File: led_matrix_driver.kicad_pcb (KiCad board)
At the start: 4 copper layers, 41 parts, among them J1 Conn_02x17_Odd_Even, Q1 PXN020-100QSJ, Q2 TPH4R50ANH1,LQ, U1 LV5144RGYR, U2 Pico, U3 ESP32-WROOM-32, U4 74AHCT541, U5 74AHCT541

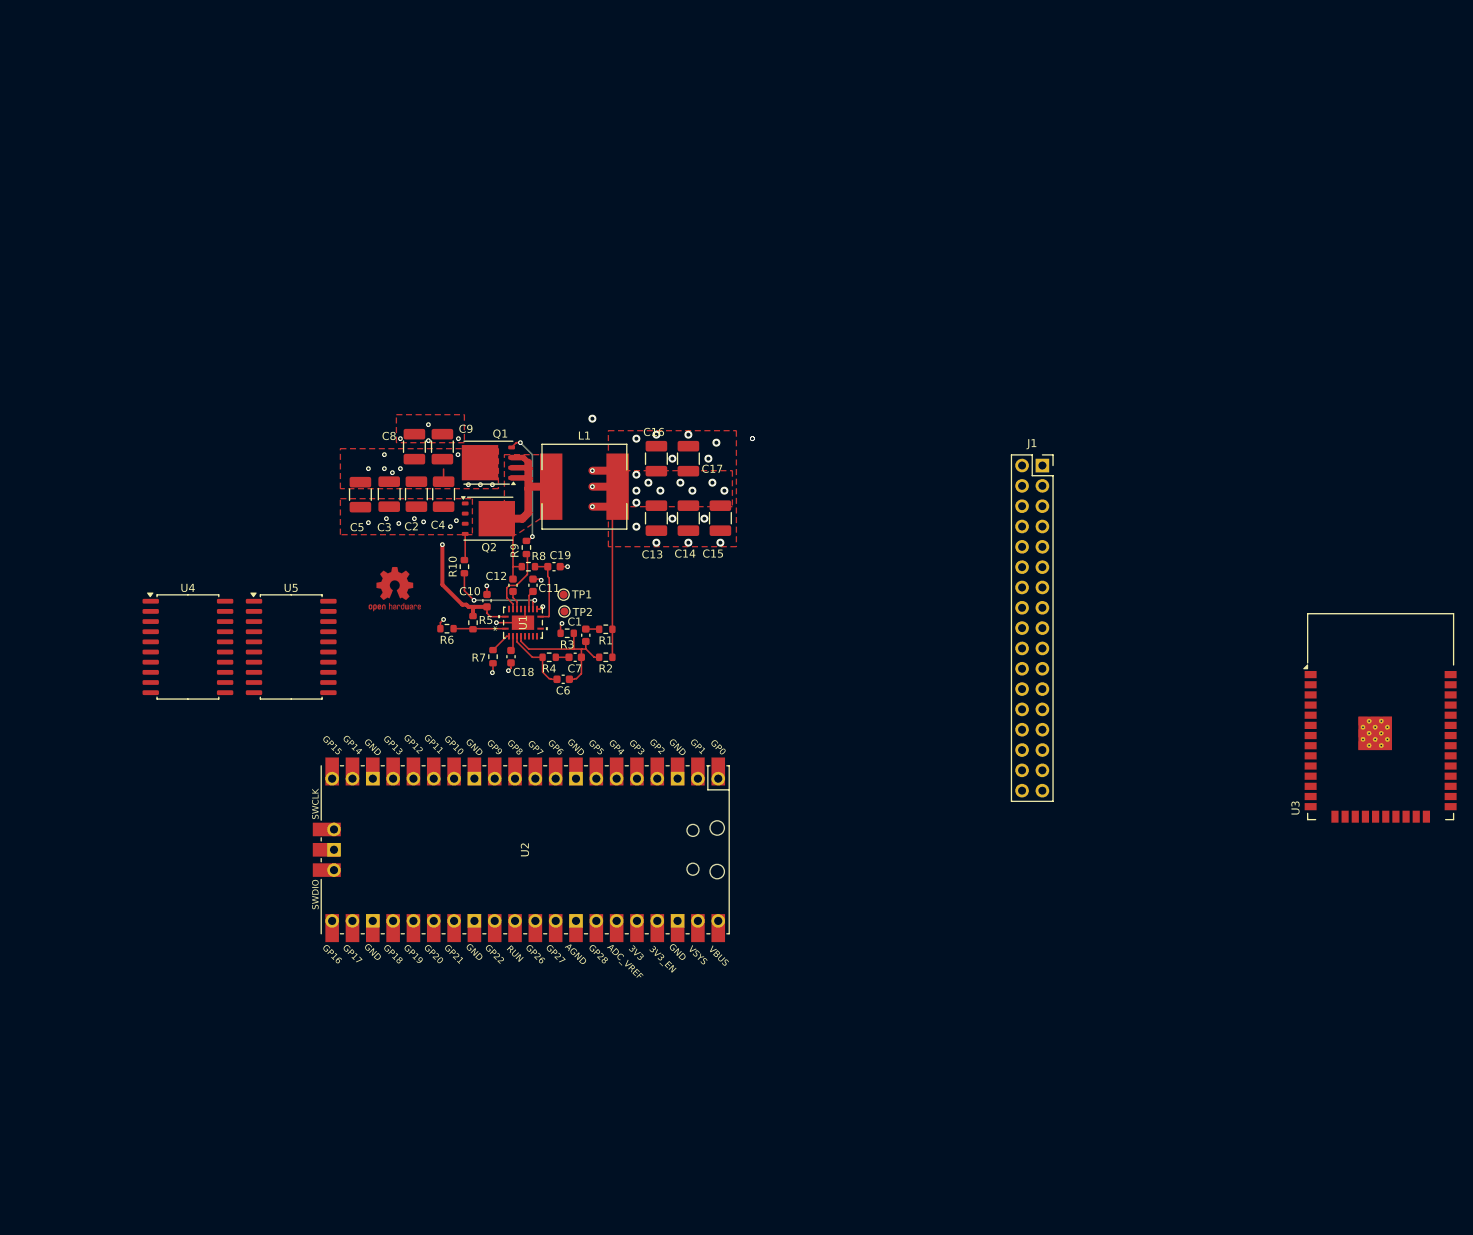
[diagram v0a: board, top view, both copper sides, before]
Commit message: Rearranged LED signals for easier layout
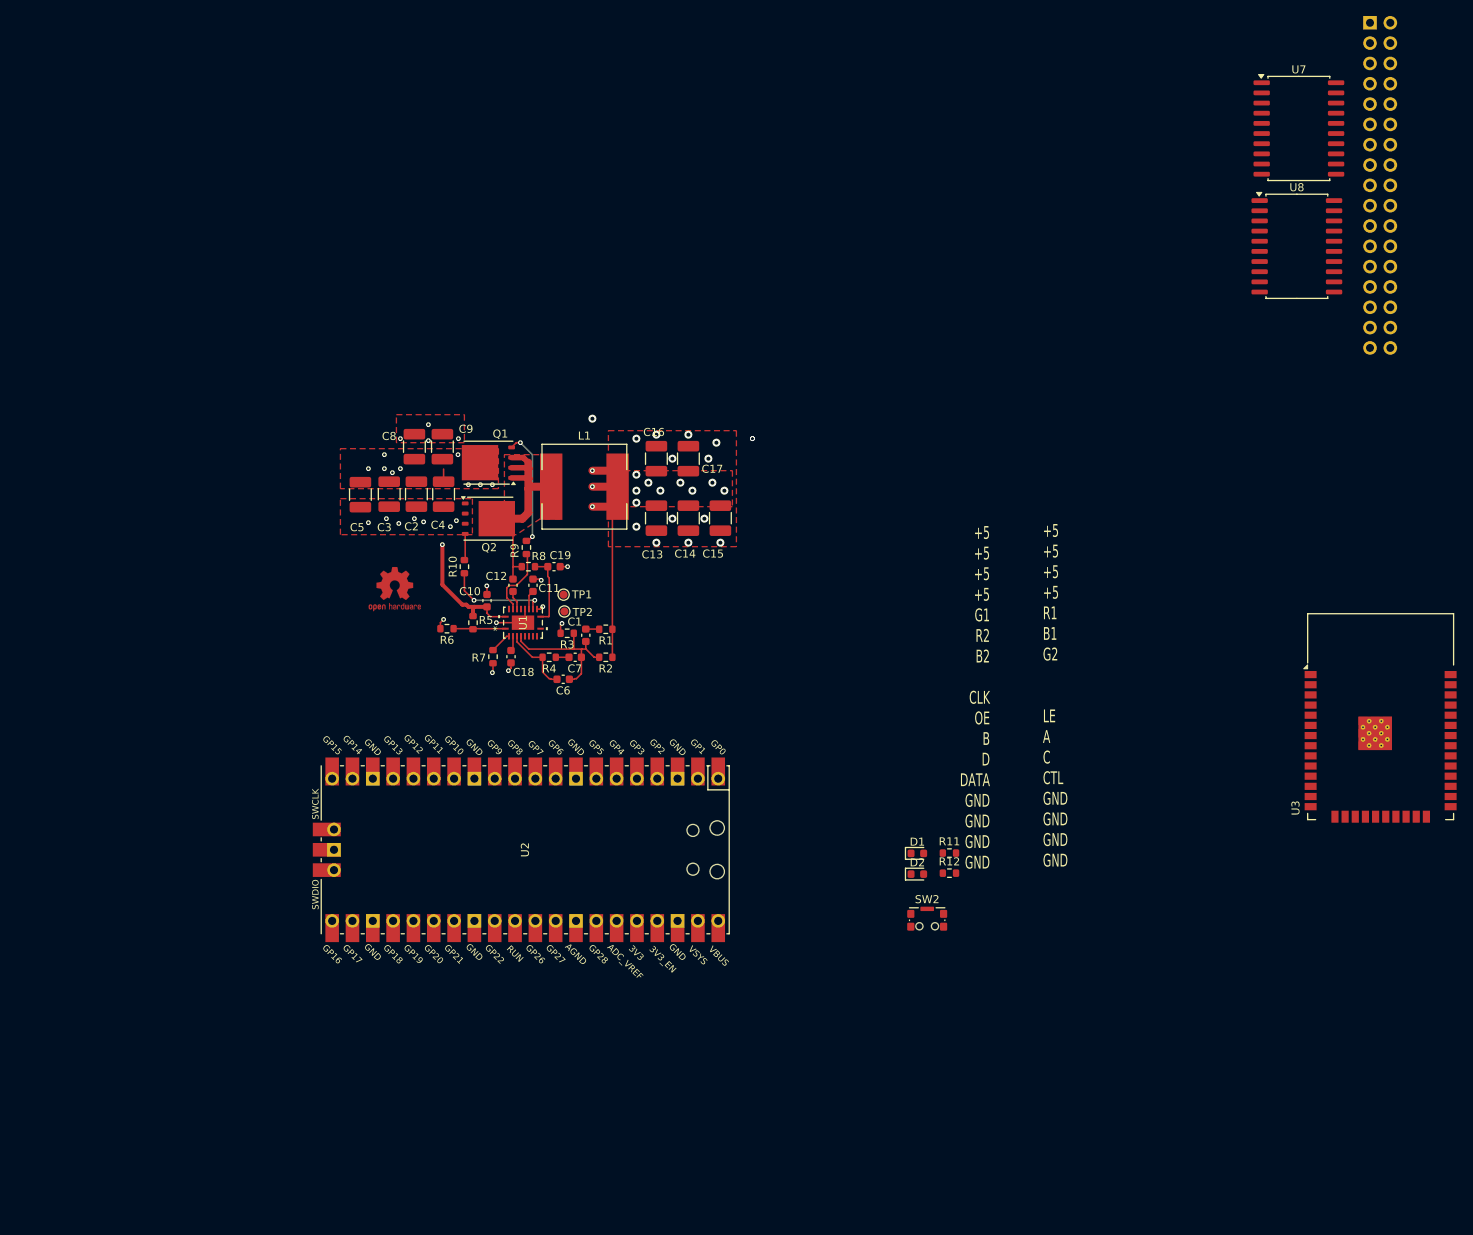
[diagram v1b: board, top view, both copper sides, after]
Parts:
- removed J1: Conn_02x17_Odd_Even, Connector_PinSocket_2.54mm:PinSocket_2x17_P2.54mm_Vertical
- removed U4, U5: 74AHCT541, Package_SO:SOIC-20W_7.5x12.8mm_P1.27mm
- added D1: LED green, LED_SMD:LED_0603_1608Metric, F.Cu at (162.6, 104.8)
- added D2: LED green, LED_SMD:LED_0603_1608Metric, F.Cu at (162.6, 107.4)
- added J5: Conn_02x17_Odd_Even, Connector_PinSocket_2.54mm:PinSocket_2x17_P2.54mm_Vertical, B.Cu at (219.2, 1.02)
- added R11: 17k8, Resistor_SMD:R_0603_1608Metric, F.Cu at (166.6, 104.8)
- added R12: 17k8, Resistor_SMD:R_0603_1608Metric, F.Cu at (166.6, 107.3)
- added SW2: CK_KMS2xxGP, Button_Switch_SMD:SW_SPST_CK_KMS2xxGP, F.Cu at (163.8, 113.2)
- added U7: 74AHCT541, Package_SO:SOIC-20W_7.5x12.8mm_P1.27mm, F.Cu at (210.3, 14.2)
- added U8: 74AHCT541, Package_SO:SOIC-20W_7.5x12.8mm_P1.27mm, F.Cu at (210.1, 29.0)
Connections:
- C13 pad 1: /48 V to 5 V power supply/V_OUT -> +5V
- C14 pad 1: /48 V to 5 V power supply/V_OUT -> +5V
- C15 pad 1: /48 V to 5 V power supply/V_OUT -> +5V
- C16 pad 1: /48 V to 5 V power supply/V_OUT -> +5V
- C17 pad 1: /48 V to 5 V power supply/V_OUT -> +5V
- L1 pad 2: /48 V to 5 V power supply/V_OUT -> +5V
- R1 pad 1: /48 V to 5 V power supply/V_OUT -> +5V
- R2 pad 1: /48 V to 5 V power supply/V_OUT -> +5V
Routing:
- net /48 V to 5 V power supply/V_OUT: track 35.4 -> 0.00 mm, vias 12 -> 0
- net +5V: track 0.00 -> 35.4 mm, vias 0 -> 12
- added copper zone on F.Cu, net +5V
- added copper zone on In2.Cu, net +5V
- removed copper zone on F.Cu, net /48 V to 5 V power supply/V_OUT
- removed copper zone on In2.Cu, net /48 V to 5 V power supply/V_OUT
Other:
- board text added: "+5 +5 +5 +5 G1 R2 B2 CLK OE B D DATA GND GND GND GND"
- board text added: "+5 +5 +5 +5 R1 B1 G2 LE A C CTL GND GND GND GND"

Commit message: Added Teensy
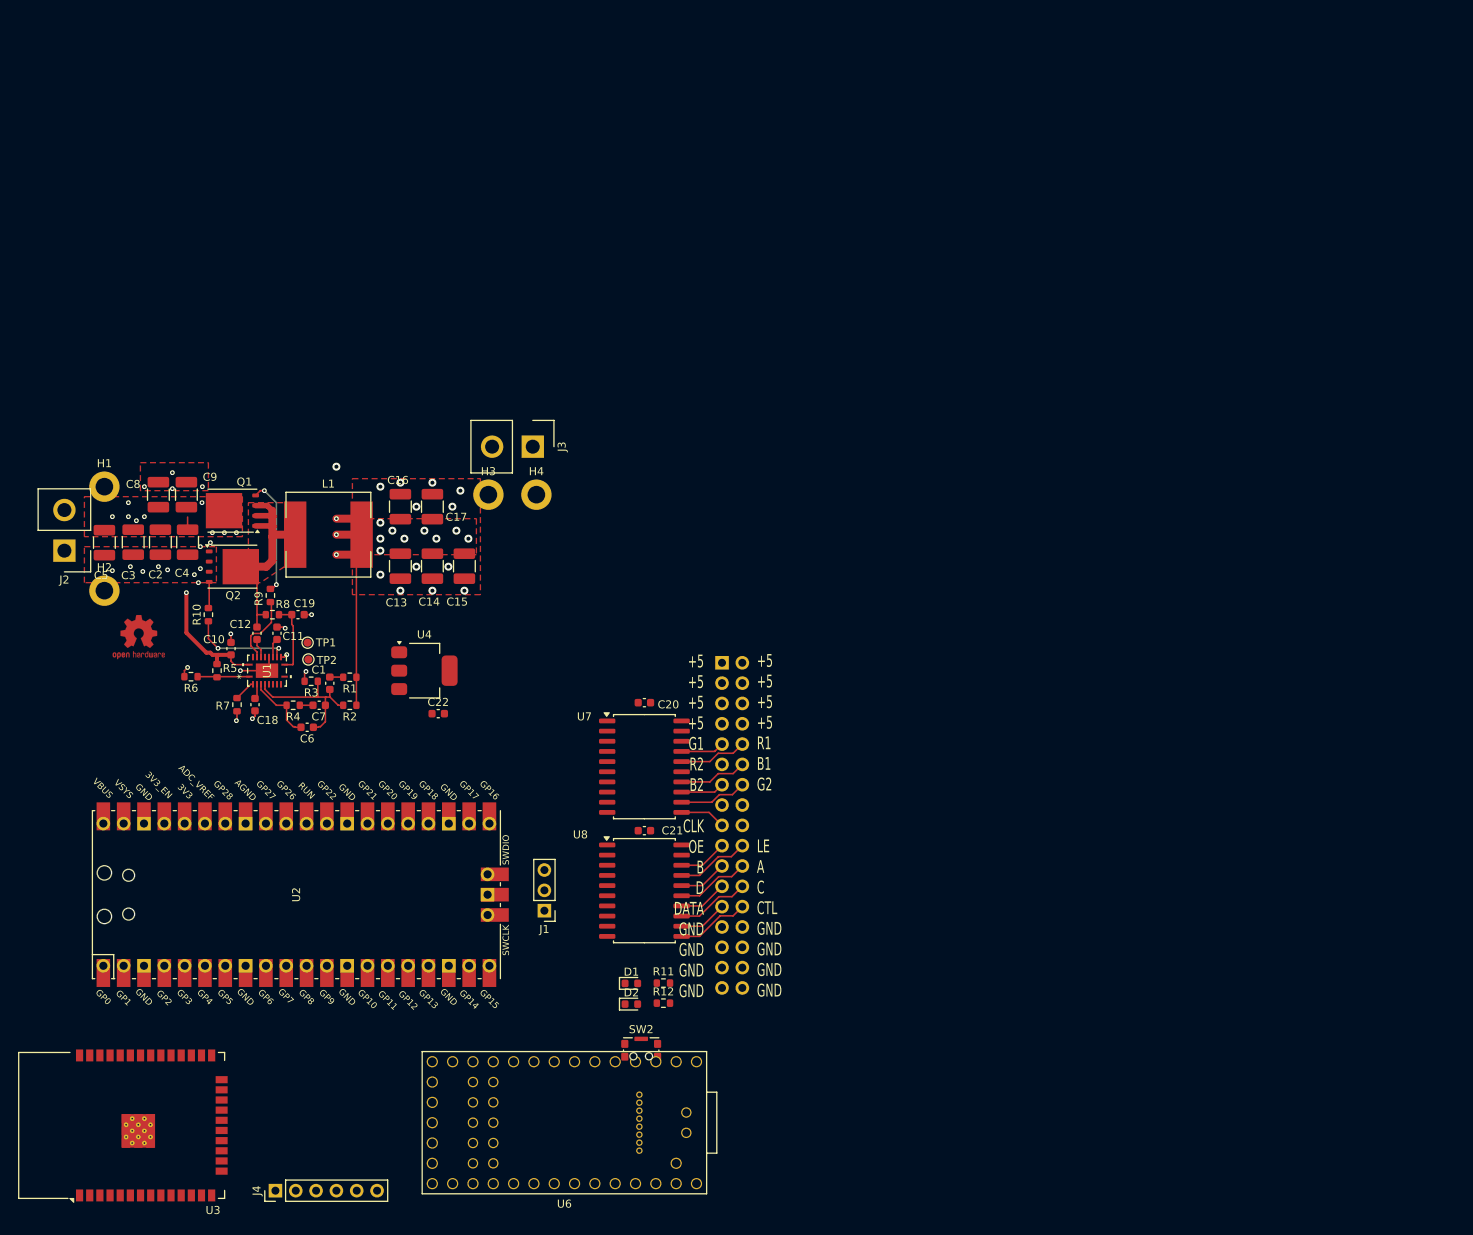
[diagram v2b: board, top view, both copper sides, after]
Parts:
- added C20: 100n, Capacitor_SMD:C_0603_1608Metric, F.Cu at (128.5, 86.0)
- added C21: 100n, Capacitor_SMD:C_0603_1608Metric, F.Cu at (128.5, 102.0)
- added C22: 100n, Capacitor_SMD:C_0603_1608Metric, F.Cu at (102.7, 87.4)
- added H1: IN+, MountingHole:MountingHole_2.2mm_M2_DIN965_Pad, F.Cu at (61.0, 59.0)
- added H2: IN-, MountingHole:MountingHole_2.2mm_M2_DIN965_Pad, F.Cu at (61.0, 72.0)
- added H3: +5V, MountingHole:MountingHole_2.2mm_M2_DIN965_Pad, F.Cu at (109.0, 60.0)
- added H4: GND, MountingHole:MountingHole_2.2mm_M2_DIN965_Pad, F.Cu at (115.0, 60.0)
- added J1: Conn_01x03_Pin, Connector_PinHeader_2.54mm:PinHeader_1x03_P2.54mm_Vertical, F.Cu at (116.0, 112.0)
- added J2: Screw_Terminal_01x02, Connector_Samtec_HPM_THT:Samtec_HPM-02-01-x-S_Straight_1x02_Pitch5.08mm, F.Cu at (56.0, 67.0)
- added J3: Screw_Terminal_01x02, Connector_Samtec_HPM_THT:Samtec_HPM-02-01-x-S_Straight_1x02_Pitch5.08mm, F.Cu at (114.5, 54.0)
- added J4: Conn_01x06_Pin, Connector_PinHeader_2.54mm:PinHeader_1x06_P2.54mm_Vertical, F.Cu at (82.4, 147.0)
- added U4: AP1117-33, Package_TO_SOT_SMD:SOT-223-3_TabPin2, F.Cu at (101.0, 82.0)
- added U6: Teensy4.0, teensy:Teensy40_SMT, F.Cu at (118.5, 138.5)
- moved U3 161.7 mm to (66.1, 138.8), turned to 90 degrees
- moved U8 114.6 mm to (128.5, 109.5)
- moved U7 114.3 mm to (128.5, 94.0)
- moved J5 113.8 mm to (138.2, 81.0)
- moved D1 39.3 mm to (126.9, 121.1)
- moved D2 39.3 mm to (126.9, 123.7)
- moved R11 39.3 mm to (130.9, 121.0)
- moved R12 39.3 mm to (130.9, 123.6)
- moved SW2 39.3 mm to (128.1, 129.4)
- moved C1 32.6 mm to (89.2, 83.6)
- moved C10 32.6 mm to (76.8, 79.2)
- moved C11 32.6 mm to (82.6, 77.3)
- moved C12 32.6 mm to (80.1, 77.3)
- moved C13 32.6 mm to (98.0, 68.9)
- moved C14 32.6 mm to (102.0, 68.9)
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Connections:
- U2 pad 1: unconnected-(U2-GPIO0-Pad1) -> /R1
- U2 pad 10: unconnected-(U2-GPIO7-Pad10) -> /LE
- U2 pad 11: unconnected-(U2-GPIO8-Pad11) -> /CTL
- U2 pad 12: unconnected-(U2-GPIO9-Pad12) -> /DATA
- U2 pad 13: unconnected-(U2-GND-Pad13) -> /A
- U2 pad 14: unconnected-(U2-GPIO10-Pad14) -> /B
- U2 pad 15: unconnected-(U2-GPIO11-Pad15) -> /C
- U2 pad 16: unconnected-(U2-GPIO12-Pad16) -> /D
- U2 pad 18: unconnected-(U2-GND-Pad18) -> GND
- U2 pad 2: unconnected-(U2-GPIO1-Pad2) -> /R2
- U2 pad 23: unconnected-(U2-GND-Pad23) -> GND
- U2 pad 28: unconnected-(U2-GND-Pad28) -> GND
- U2 pad 3: unconnected-(U2-GND-Pad3) -> GND
- U2 pad 38: unconnected-(U2-GND-Pad38) -> GND
- U2 pad 39: unconnected-(U2-VSYS-Pad39) -> +5V
- U2 pad 4: unconnected-(U2-GPIO2-Pad4) -> /G1
- U2 pad 41: unconnected-(U2-SWCLK-Pad41) -> Net-(J1-Pin_1)
- U2 pad 42: unconnected-(U2-GND-Pad42) -> Net-(J1-Pin_2)
- U2 pad 43: unconnected-(U2-SWDIO-Pad43) -> Net-(J1-Pin_3)
- U2 pad 5: unconnected-(U2-GPIO3-Pad5) -> /G2
- U2 pad 6: unconnected-(U2-GPIO4-Pad6) -> /B1
- U2 pad 7: unconnected-(U2-GPIO5-Pad7) -> /B2
- U2 pad 8: unconnected-(U2-GND-Pad8) -> GND
- U2 pad 9: unconnected-(U2-GPIO6-Pad9) -> /CLK
- U3 pad 1: Net-(U3-GND-Pad1) -> GND
- U3 pad 15: Net-(U3-GND-Pad1) -> GND
- U3 pad 2: unconnected-(U3-VDD-Pad2) -> +3V3
- U3 pad 38: Net-(U3-GND-Pad1) -> GND
- U3 pad 39: Net-(U3-GND-Pad1) -> GND
- U7 pad 1: unconnected-(U7-G1-Pad1) -> GND
- U7 pad 10: unconnected-(U7-GND-Pad10) -> GND
- U7 pad 19: unconnected-(U7-G2-Pad19) -> GND
- U7 pad 20: unconnected-(U7-VCC-Pad20) -> +5V
- U7 pad 3: unconnected-(U7-A1-Pad3) -> /G1
- U7 pad 4: unconnected-(U7-A2-Pad4) -> /R1
- U7 pad 5: unconnected-(U7-A3-Pad5) -> /R2
- U7 pad 6: unconnected-(U7-A4-Pad6) -> /B1
- U7 pad 7: unconnected-(U7-A5-Pad7) -> /B2
- U7 pad 8: unconnected-(U7-A6-Pad8) -> /G2
- U7 pad 9: unconnected-(U7-A7-Pad9) -> /CLK
- U8 pad 1: unconnected-(U8-G1-Pad1) -> GND
- U8 pad 10: unconnected-(U8-GND-Pad10) -> GND
- U8 pad 19: unconnected-(U8-G2-Pad19) -> GND
- U8 pad 2: unconnected-(U8-A0-Pad2) -> /OE
- U8 pad 20: unconnected-(U8-VCC-Pad20) -> +5V
- U8 pad 3: unconnected-(U8-A1-Pad3) -> /LE
- U8 pad 4: unconnected-(U8-A2-Pad4) -> /B
- U8 pad 5: unconnected-(U8-A3-Pad5) -> /A
- U8 pad 6: unconnected-(U8-A4-Pad6) -> /D
- U8 pad 7: unconnected-(U8-A5-Pad7) -> /C
- U8 pad 8: unconnected-(U8-A6-Pad8) -> /DATA
- U8 pad 9: unconnected-(U8-A7-Pad9) -> /CTL
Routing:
- net /LED_CTL: track 0.00 -> 9.13 mm
- net /LED_A: track 0.00 -> 9.13 mm
- net /LED_C: track 0.00 -> 9.13 mm
- net /LED_LE: track 0.00 -> 9.13 mm
- net /LED_DB1: track 0.00 -> 8.50 mm
- net /LED_DR1: track 0.00 -> 8.50 mm
- net /LED_DG2: track 0.00 -> 8.50 mm
- net /LED_OE: track 0.00 -> 6.07 mm
- net /LED_DATA: track 0.00 -> 6.07 mm
- net /LED_D: track 0.00 -> 6.07 mm
- net /LED_B: track 0.00 -> 6.07 mm
- net /LED_CLK: track 0.00 -> 5.72 mm
- net /LED_DG1: track 0.00 -> 5.43 mm
- net /LED_DB2: track 0.00 -> 5.43 mm
- net GND: vias 33 -> 36
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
